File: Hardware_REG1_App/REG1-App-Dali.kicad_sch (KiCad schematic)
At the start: 26 parts, among them J1 REG1_App_Connector, J3 DALI, Q1 BSS123, Q2 BC857, U1 EL357N(A)(TA)-G, U2 EL357N(A)(TA)-G, U3 STN93003, U4 STN1HNK60

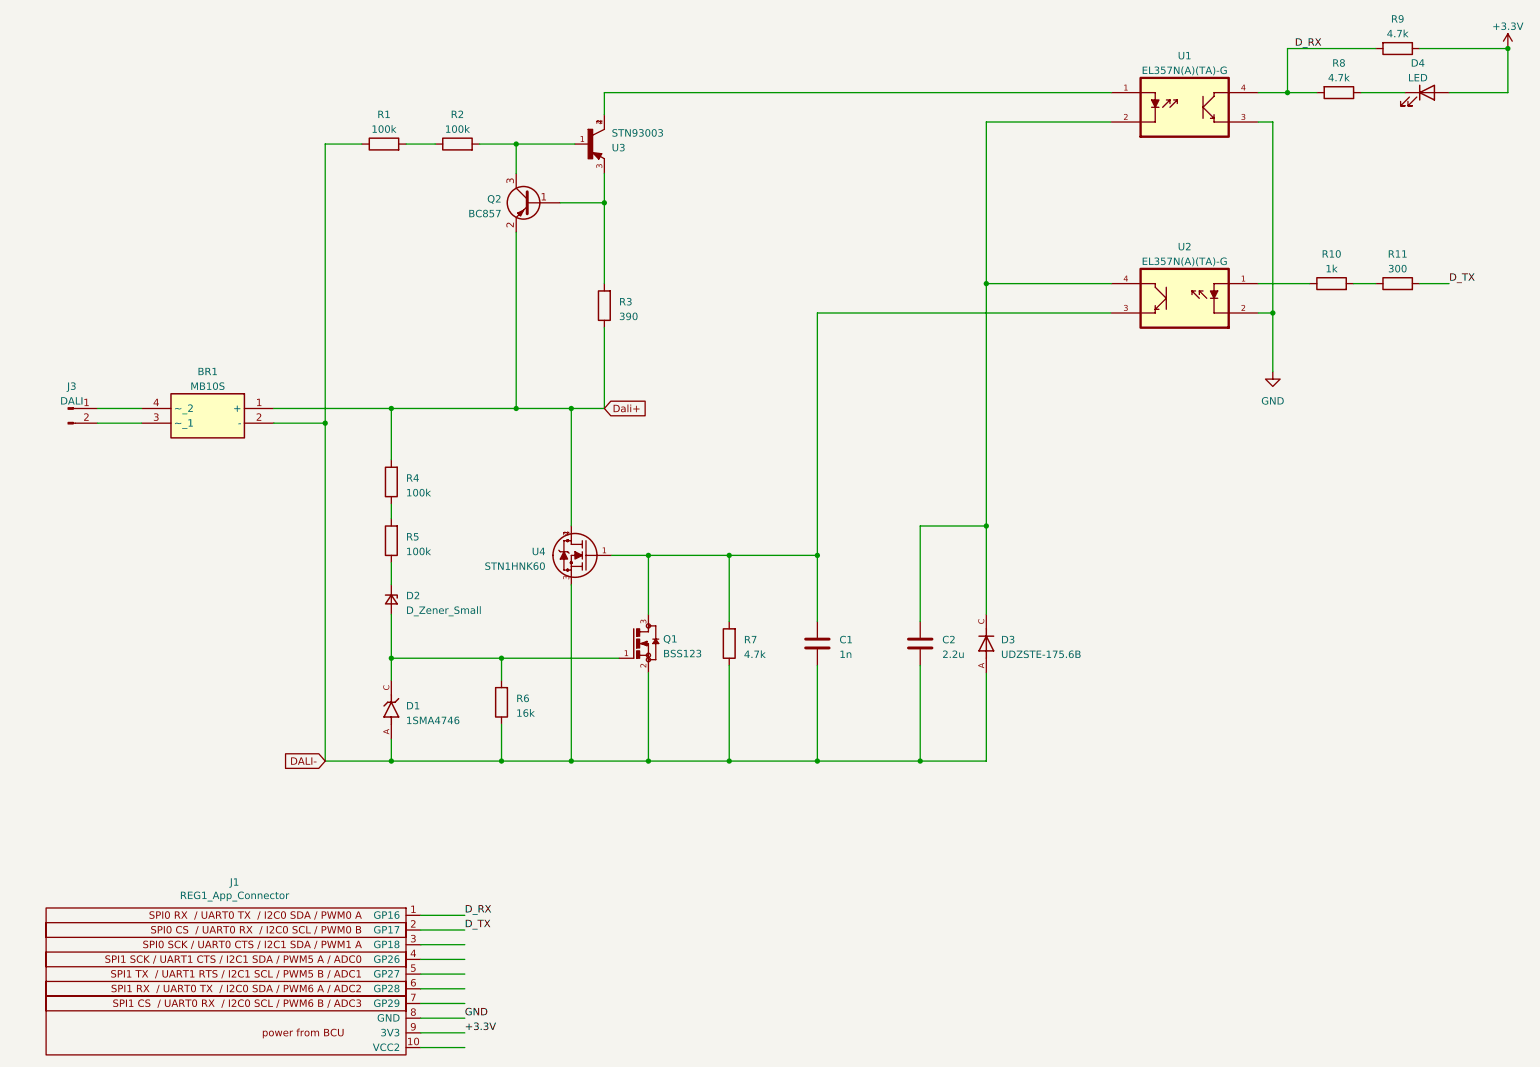
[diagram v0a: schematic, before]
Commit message: updated REG1 and renamed
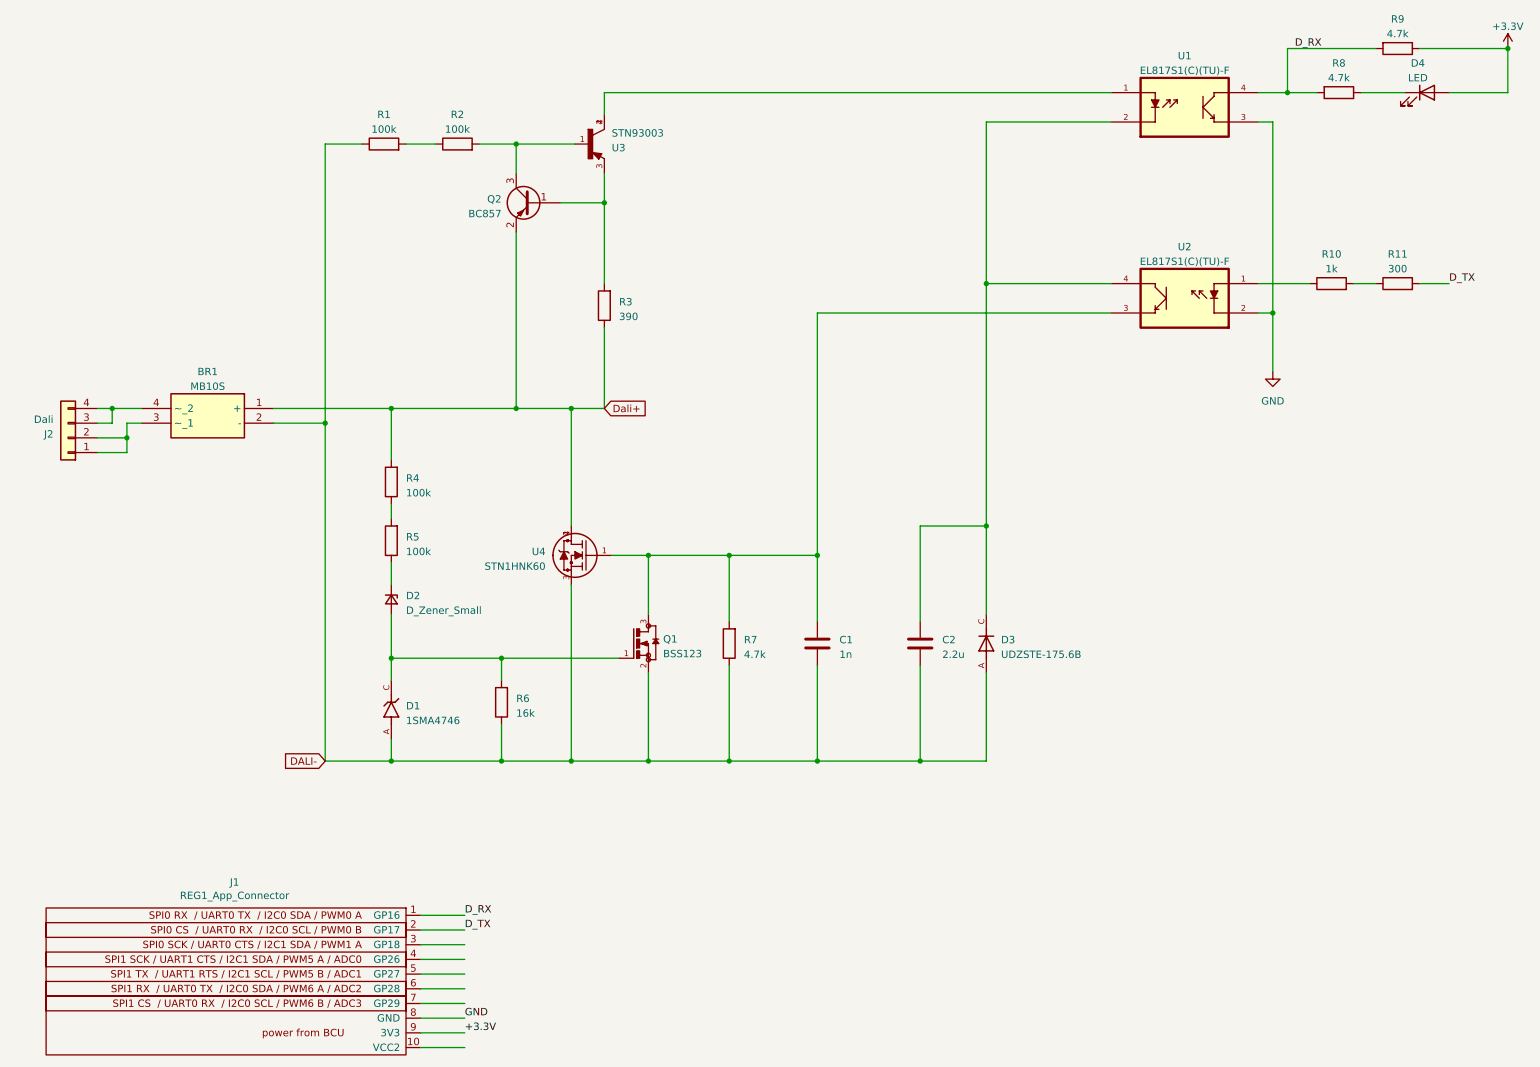
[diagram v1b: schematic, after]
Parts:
- removed J3: DALI, TerminalBlock_4Ucon:TerminalBlock_4Ucon_1x02_P3.50mm_Horizontal, symbol Connector:Conn_01x02_Pin
- added J2: Dali, Connector_Phoenix_MC:PhoenixContact_MC_1,5_4-G-3.5_1x04_P3.50mm_Horizontal, symbol Connector_Generic:Conn_01x04
- U1, U2: value EL357N(A)(TA)-G -> EL817S1(C)(TU)-F; footprint SOP254P700X200-4N -> DALI:SOIC254P1030X390-4N
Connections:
- net at BR1.3 (~_1): now also J2.1 (Pin_1), J2.2 (Pin_2)
- net at BR1.4 (~_2): now also J2.3 (Pin_3), J2.4 (Pin_4)
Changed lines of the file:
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@@
   (junction (at 78.74 80.01) (diameter 0) (color 0 0 0 0)
   )
+  (junction (at 30.48 80.01) (diameter 0) (color 0 0 0 0)
+  )
   (junction (at 100.33 80.01) (diameter 0) (color 0 0 0 0)
   )
@@
   (junction (at 97.79 140.97) (diameter 0) (color 0 0 0 0)
   )
+  (junction (at 33.02 85.09) (diameter 0) (color 0 0 0 0)
+  )
   (junction (at 137.16 105.41) (diameter 0) (color 0 0 0 0)
   )
@@
     (stroke (width 0) (type default))
   )
+  (wire (pts (xy 27.94 85.09) (xy 33.02 85.09))
+    (stroke (width 0) (type default))
+  )
   (wire (pts (xy 109.855 140.97) (xy 123.19 140.97))
     (stroke (width 0) (type default))
@@
     (stroke (width 0) (type default))
   )
-  (wire (pts (xy 27.94 82.55) (xy 35.56 82.55))
-    (stroke (width 0) (type default))
-  )
   (wire (pts (xy 91.44 175.26) (xy 83.82 175.26))
     (stroke (width 0) (type default))
@@
     (stroke (width 0) (type default))
   )
+  (wire (pts (xy 30.48 80.01) (xy 35.56 80.01))
+    (stroke (width 0) (type default))
+  )
   (wire (pts (xy 115.57 44.45) (xy 115.57 58.42))
     (stroke (width 0) (type default))
@@
     (stroke (width 0) (type default))
   )
+  (wire (pts (xy 30.48 82.55) (xy 30.48 80.01))
+    (stroke (width 0) (type default))
+  )
   (wire (pts (xy 78.74 123.19) (xy 78.74 127))
     (stroke (width 0) (type default))
@@
     (stroke (width 0) (type default))
   )
+  (wire (pts (xy 35.56 82.55) (xy 33.02 82.55))
+    (stroke (width 0) (type default))
+  )
+  (wire (pts (xy 27.94 82.55) (xy 30.48 82.55))
+    (stroke (width 0) (type default))
+  )
   (wire (pts (xy 91.44 180.34) (xy 83.82 180.34))
     (stroke (width 0) (type default))
@@
     (stroke (width 0) (type default))
   )
+  (wire (pts (xy 33.02 87.63) (xy 27.94 87.63))
+    (stroke (width 0) (type default))
+  )
   (wire (pts (xy 97.79 134.62) (xy 97.79 140.97))
     (stroke (width 0) (type default))
@@
     (stroke (width 0) (type default))
   )
+  (wire (pts (xy 33.02 85.09) (xy 33.02 87.63))
+    (stroke (width 0) (type default))
+  )
   (wire (pts (xy 97.79 123.19) (xy 78.74 123.19))
     (stroke (width 0) (type default))
@@
     (stroke (width 0) (type default))
   )
-  (wire (pts (xy 27.94 80.01) (xy 35.56 80.01))
+  (wire (pts (xy 27.94 80.01) (xy 30.48 80.01))
     (stroke (width 0) (type default))
   )
@@
   )
   (wire (pts (xy 137.16 105.41) (xy 123.19 105.41))
+    (stroke (width 0) (type default))
+  )
+  (wire (pts (xy 33.02 82.55) (xy 33.02 85.09))
     (stroke (width 0) (type default))
   )
@@
     )
   )
+  (symbol (lib_id "Connector_Generic:Conn_01x04") (at 22.86 85.09 180) (unit 1)
+    (in_bom yes) (on_board yes) (dnp no)
+    (property "Reference" "J2" (at 20.32 84.455 0)
+      (effects (font (size 1.27 1.27)) (justify left))
+    )
+    (property "Value" "Dali" (at 20.32 81.915 0)
+      (effects (font (size 1.27 1.27)) (justify left))
+    )
+    (property "Footprint" "Connector_Phoenix_MC:PhoenixContact_MC_1,5_4-G-3.5_1x04_P3.50mm_Horizontal" (at 22.86 85.09 0)
+      (effects (font (size 1.27 1.27)) hide)
+    )
+    (property "Datasheet" "~" (at 22.86 85.09 0)
+      (effects (font (size 1.27 1.27)) hide)
+    )
+    (pin "1")
+    (pin "2")
+    (pin "3")
+    (pin "4")
+    (instances
+      (project "REG1-App-Universal"
+        (path "/a0393b09-4b2d-4a64-98b7-96bb7f245f9d"
+          (reference "J2") (unit 1)
+        )
+      )
+    )
+  )
   (symbol (lib_id "DALI:STN1HNK60") (at 111.76 105.41 0) (mirror y) (unit 1)
     (in_bom yes) (on_board yes) (dnp no)
@@
       (effects (font (size 1.27 1.27)))
     )
-    (property "Value" "EL357N(A)(TA)-G" (at 215.9 54.61 0)
-      (effects (font (size 1.27 1.27)))
-    )
-    (property "Footprint" "SOP254P700X200-4N" (at 215.9 60.96 0)
+    (property "Value" "EL817S1(C)(TU)-F" (at 215.9 54.61 0)
+      (effects (font (size 1.27 1.27)))
+    )
+    (property "Footprint" "DALI:SOIC254P1030X390-4N" (at 215.9 60.96 0)
       (effects (font (size 1.27 1.27)) (justify bottom) hide)
     )
@@
     )
   )
-  (symbol (lib_id "Connector:Conn_01x02_Pin") (at 22.86 80.01 0) (unit 1)
-    (in_bom yes) (on_board yes) (dnp no) (fields_autoplaced)
-    (property "Reference" "J3" (at 23.495 76.2 0)
-      (effects (font (size 1.27 1.27)))
-    )
-    (property "Value" "DALI" (at 23.495 78.74 0)
-      (effects (font (size 1.27 1.27)))
-    )
-    (property "Footprint" "TerminalBlock_4Ucon:TerminalBlock_4Ucon_1x02_P3.50mm_Horizontal" (at 22.86 80.01 0)
-      (effects (font (size 1.27 1.27)) hide)
-    )
-    (property "Datasheet" "~" (at 22.86 80.01 0)
-      (effects (font (size 1.27 1.27)) hide)
-    )
-    (pin "1")
-    (pin "2")
-    (instances
-      (project "REG1-App-Universal"
-        (path "/a0393b09-4b2d-4a64-98b7-96bb7f245f9d"
-          (reference "J3") (unit 1)
-        )
-      )
-    )
-  )
   (symbol (lib_id "Device:C") (at 152.4 120.65 0) (unit 1)
     (in_bom yes) (on_board yes) (dnp no) (fields_autoplaced)
@@
       (effects (font (size 1.27 1.27)))
     )
-    (property "Value" "EL357N(A)(TA)-G" (at 215.9 21.59 0)
-      (effects (font (size 1.27 1.27)))
-    )
-    (property "Footprint" "SOP254P700X200-4N" (at 215.9 27.94 0)
-      (effects (font (size 1.27 1.27)) (justify bottom) hide)
-    )
+    (property "Value" "EL817S1(C)(TU)-F" (at 215.9 21.59 0)
+      (effects (font (size 1.27 1.27)))
+    )
+    (property "Footprint" "DALI:SOIC254P1030X390-4N" (at 215.9 27.94 0)
+      (effects (font (size 1.27 1.27)) (justify bottom) hide)
+    )

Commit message: updated pcb
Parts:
- U4: footprint SOT-223 -> DALI:SOT-223
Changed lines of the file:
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@@
     (pin "9")
     (instances
-      (project "REG1-App-Universal"
+      (project "REG1-App-Dali"
         (path "/a0393b09-4b2d-4a64-98b7-96bb7f245f9d"
           (reference "J1") (unit 1)
@@
     (pin "2")
     (instances
-      (project "REG1-App-Universal"
+      (project "REG1-App-Dali"
         (path "/a0393b09-4b2d-4a64-98b7-96bb7f245f9d"
           (reference "R3") (unit 1)
@@
     (pin "2")
     (instances
-      (project "REG1-App-Universal"
+      (project "REG1-App-Dali"
         (path "/a0393b09-4b2d-4a64-98b7-96bb7f245f9d"
           (reference "C2") (unit 1)
@@
     (pin "2")
     (instances
-      (project "REG1-App-Universal"
+      (project "REG1-App-Dali"
         (path "/a0393b09-4b2d-4a64-98b7-96bb7f245f9d"
           (reference "R6") (unit 1)
@@
     (pin "2")
     (instances
-      (project "REG1-App-Universal"
+      (project "REG1-App-Dali"
         (path "/a0393b09-4b2d-4a64-98b7-96bb7f245f9d"
           (reference "R5") (unit 1)
@@
     (pin "3")
     (instances
-      (project "REG1-App-Universal"
+      (project "REG1-App-Dali"
         (path "/a0393b09-4b2d-4a64-98b7-96bb7f245f9d"
           (reference "Q2") (unit 1)
@@
     (pin "2")
     (instances
-      (project "REG1-App-Universal"
+      (project "REG1-App-Dali"
         (path "/a0393b09-4b2d-4a64-98b7-96bb7f245f9d"
           (reference "R10") (unit 1)
@@
     (pin "2")
     (instances
-      (project "REG1-App-Universal"
+      (project "REG1-App-Dali"
         (path "/a0393b09-4b2d-4a64-98b7-96bb7f245f9d"
           (reference "R9") (unit 1)
@@
     (pin "2")
     (instances
-      (project "REG1-App-Universal"
+      (project "REG1-App-Dali"
         (path "/a0393b09-4b2d-4a64-98b7-96bb7f245f9d"
           (reference "D4") (unit 1)
@@
     (pin "4")
     (instances
-      (project "REG1-App-Universal"
+      (project "REG1-App-Dali"
         (path "/a0393b09-4b2d-4a64-98b7-96bb7f245f9d"
           (reference "J2") (unit 1)
@@
       (effects (font (size 1.27 1.27)) (justify left))
     )
-    (property "Footprint" "SOT-223" (at 111.76 105.41 0)
+    (property "Footprint" "DALI:SOT-223" (at 111.76 105.41 0)
       (effects (font (size 1.27 1.27)) (justify bottom) hide)
     )
@@
     (pin "4")
     (instances
-      (project "REG1-App-Universal"
+      (project "REG1-App-Dali"
         (path "/a0393b09-4b2d-4a64-98b7-96bb7f245f9d"
           (reference "U4") (unit 1)
@@
     (pin "2")
     (instances
-      (project "REG1-App-Universal"
+      (project "REG1-App-Dali"
         (path "/a0393b09-4b2d-4a64-98b7-96bb7f245f9d"
           (reference "R8") (unit 1)
@@
     (pin "4")
     (instances
-      (project "REG1-App-Universal"
+      (project "REG1-App-Dali"
         (path "/a0393b09-4b2d-4a64-98b7-96bb7f245f9d"
           (reference "U2") (unit 1)
@@
     (pin "2")
     (instances
-      (project "REG1-App-Universal"
+      (project "REG1-App-Dali"
         (path "/a0393b09-4b2d-4a64-98b7-96bb7f245f9d"
           (reference "R4") (unit 1)
@@
     (pin "4")
     (instances
-      (project "REG1-App-Universal"
+      (project "REG1-App-Dali"
         (path "/a0393b09-4b2d-4a64-98b7-96bb7f245f9d"
           (reference "U3") (unit 1)
@@
     (pin "C")
     (instances
-      (project "REG1-App-Universal"
+      (project "REG1-App-Dali"
         (path "/a0393b09-4b2d-4a64-98b7-96bb7f245f9d"
           (reference "D3") (unit 1)
@@
     (pin "4")
     (instances
-      (project "REG1-App-Universal"
+      (project "REG1-App-Dali"
         (path "/a0393b09-4b2d-4a64-98b7-96bb7f245f9d"
           (reference "BR1") (unit 1)
@@
     (pin "2")
     (instances
-      (project "REG1-App-Universal"
+      (project "REG1-App-Dali"
         (path "/a0393b09-4b2d-4a64-98b7-96bb7f245f9d"
           (reference "C1") (unit 1)
@@
     (pin "2")
     (instances
-      (project "REG1-App-Universal"
+      (project "REG1-App-Dali"
         (path "/a0393b09-4b2d-4a64-98b7-96bb7f245f9d"
           (reference "R7") (unit 1)
@@
     (pin "4")
     (instances
-      (project "REG1-App-Universal"
+      (project "REG1-App-Dali"
         (path "/a0393b09-4b2d-4a64-98b7-96bb7f245f9d"
           (reference "U1") (unit 1)
@@
     (pin "2")
     (instances
-      (project "REG1-App-Universal"
+      (project "REG1-App-Dali"
         (path "/a0393b09-4b2d-4a64-98b7-96bb7f245f9d"
           (reference "R2") (unit 1)
@@
     (pin "2")
     (instances
-      (project "REG1-App-Universal"
+      (project "REG1-App-Dali"
         (path "/a0393b09-4b2d-4a64-98b7-96bb7f245f9d"
           (reference "R11") (unit 1)
@@
     (pin "3")
     (instances
-      (project "REG1-App-Universal"
+      (project "REG1-App-Dali"
         (path "/a0393b09-4b2d-4a64-98b7-96bb7f245f9d"
           (reference "Q1") (unit 1)
@@
     (pin "1")
     (instances
-      (project "REG1-App-Universal"
+      (project "REG1-App-Dali"
         (path "/a0393b09-4b2d-4a64-98b7-96bb7f245f9d"
           (reference "#PWR02") (unit 1)
@@
     (pin "2")
     (instances
-      (project "REG1-App-Universal"
+      (project "REG1-App-Dali"
         (path "/a0393b09-4b2d-4a64-98b7-96bb7f245f9d"
           (reference "R1") (unit 1)
@@
     (pin "2")
     (instances
-      (project "REG1-App-Universal"
+      (project "REG1-App-Dali"
         (path "/a0393b09-4b2d-4a64-98b7-96bb7f245f9d"
           (reference "D2") (unit 1)
@@
     (pin "1")
     (instances
-      (project "REG1-App-Universal"
+      (project "REG1-App-Dali"
         (path "/a0393b09-4b2d-4a64-98b7-96bb7f245f9d"
           (reference "#PWR01") (unit 1)
@@
     (pin "C")
     (instances
-      (project "REG1-App-Universal"
+      (project "REG1-App-Dali"
         (path "/a0393b09-4b2d-4a64-98b7-96bb7f245f9d"
           (reference "D1") (unit 1)
